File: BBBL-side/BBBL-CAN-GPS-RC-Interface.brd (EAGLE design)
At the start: 50.8 x 48.3 mm, 14 parts, among them IC2 74AUC1G06DBV

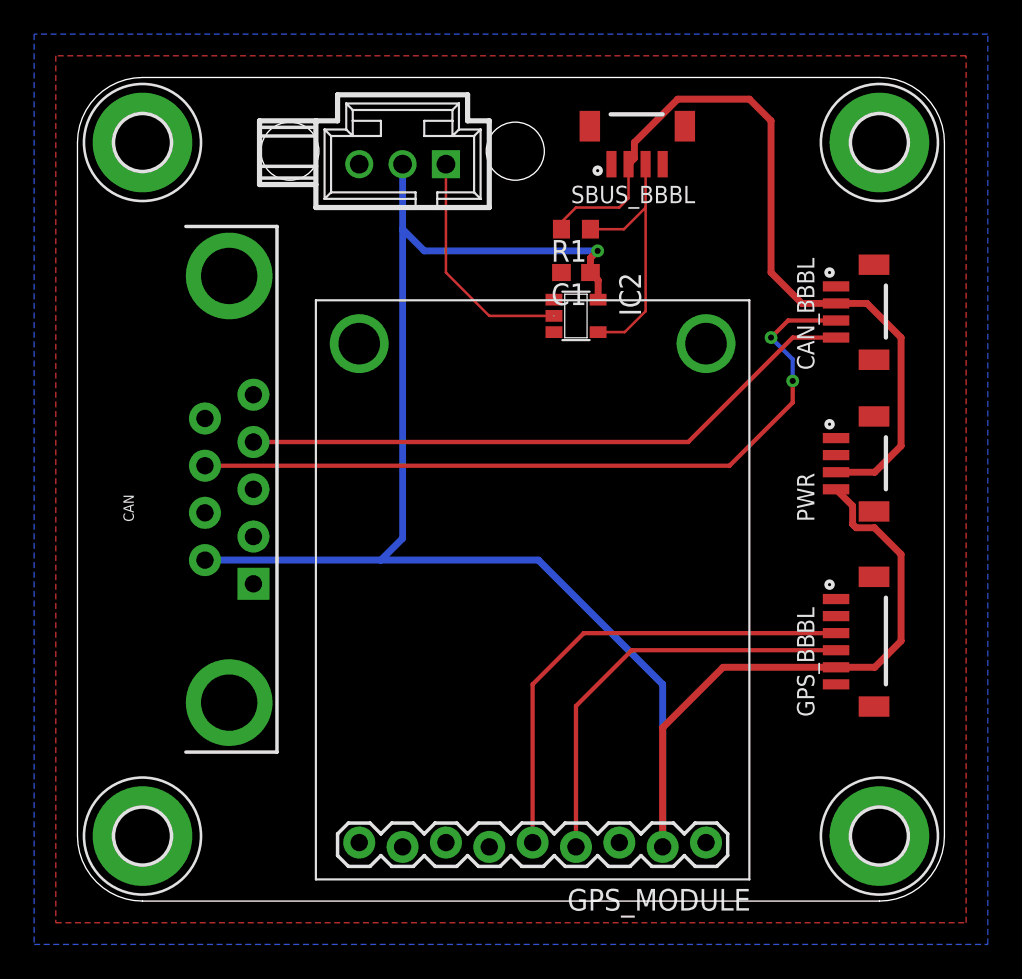
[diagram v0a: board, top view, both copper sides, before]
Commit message: Moved original interface board and added a new interface board for plugging a Pololu dual VNH5019 shield into a stack
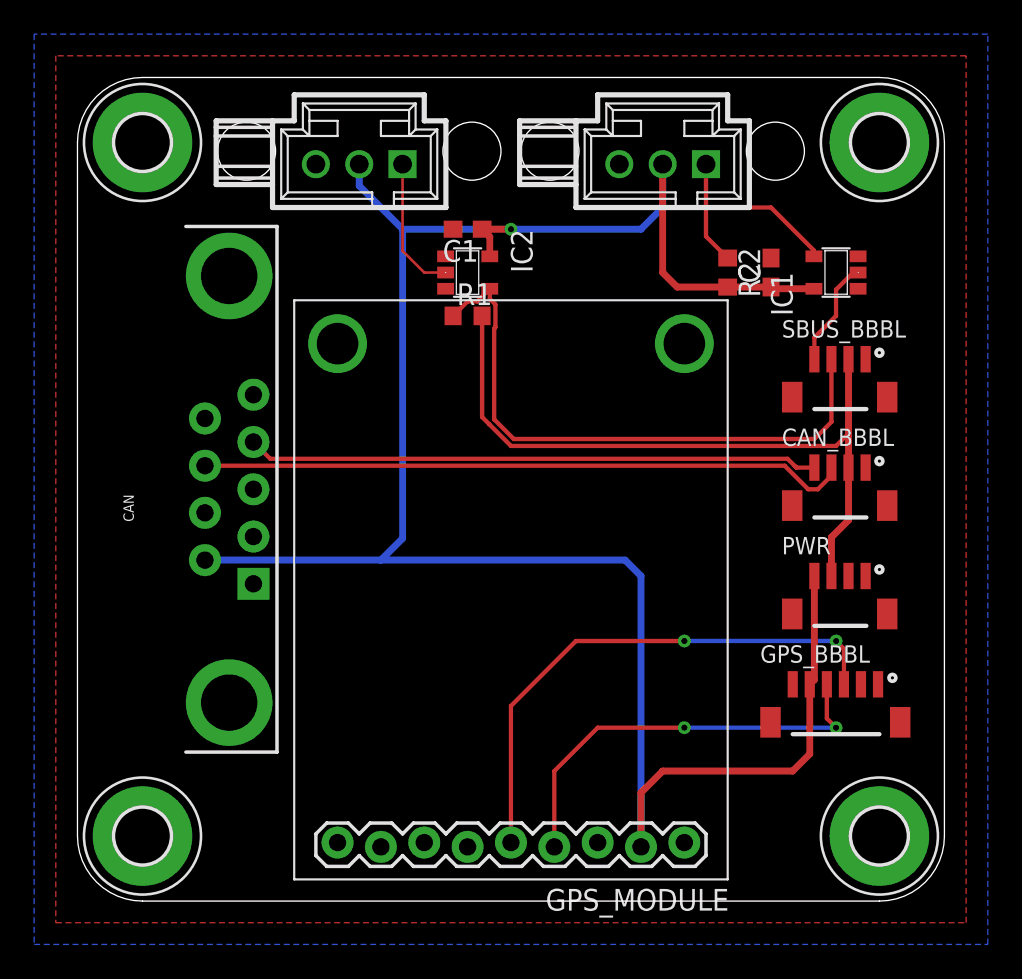
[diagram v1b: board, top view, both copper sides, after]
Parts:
- removed SBUS: HEADER_POS3_70545, con-molex-c-grid-sl:70545-POS3
- added C2: 100n, resistor:C0603
- added IC1: 74AUC1G06DBV, 74xx-little-us:SOT23-5
- added R2: 4k7, resistor:R0603
- added SBUS_IN, SBUS_OUT: HEADER_POS3_70545, con-molex-c-grid-sl:70545-POS3
- moved SBUS_BBBL 19.8 mm to (45.7, 30.5), turned to 0 degrees
- moved CAN_BBBL 11.4 mm to (45.7, 24.1), turned to 0 degrees
- moved PWR 8.89 mm to (45.7, 17.8), turned to 0 degrees
- moved R1 8.13 mm to (22.9, 34.3), turned to 0 degrees
- moved C1 6.84 mm to (22.9, 39.4)
- moved IC2 6.84 mm to (22.9, 36.8)
- moved GPS_BBBL 2.54 mm to (41.9, 12.7), turned to 0 degrees
- moved GPS_MODULE 1.27 mm to (12.7, 1.27)
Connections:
- new net N$7: IC1.4, R2.1, SBUS_OUT.P$1
- new net N$8: IC1.2, SBUS_BBBL.4
- net +5V: now also C2.1, IC1.5, R2.2, SBUS_IN.P$2, SBUS_OUT.P$2; no longer SBUS.P$2
- net GND: now also C2.2, IC1.3, SBUS_IN.P$3, SBUS_OUT.P$3; no longer SBUS.P$3
- net N$6: now also SBUS_IN.P$1; no longer SBUS.P$1
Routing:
- net N$5: track 15.7 -> 35.0 mm
- net +5V: track 112.4 -> 128.4 mm
- net N$7: track 0.00 -> 13.9 mm
- net N$3: track 44.5 -> 38.1 mm, vias 2 -> 0
- net N$8: track 0.00 -> 6.31 mm
- net N$6: track 13.7 -> 8.13 mm
- net +3V3: track 46.8 -> 42.1 mm
- net N$1: track 28.3 -> 31.4 mm, vias 0 -> 2
- net N$4: track 36.7 -> 33.6 mm
- net N$2: vias 0 -> 2
